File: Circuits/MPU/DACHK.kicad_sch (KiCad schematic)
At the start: 29 parts, among them J12 Conn_02x03_Odd_Even, U1 ProASIC, U11 AD5328, U12 MAX308CSE+, U13 MAX308CSE+, U14 ADA4805-2ARMZ, U15 AD7984BRMZ

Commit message: LVDS I/F for HV
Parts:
- U1: desc FPGA -> FPGA; manf# (none) -> A3PE3000-FGG484
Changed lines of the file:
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@@
 			)
 		)
-		(property "Datasheet" "	https://www.microsemi.com/document-portal/doc_download/130701-ds0098-proasic3e-flash-family-fpgas-datasheet"
+		(property "Datasheet" "https://www.microsemi.com/document-portal/doc_download/130701-ds0098-proasic3e-flash-family-fpgas-datasheet"
 			(at 30.48 87.63 0)
 			(effects
@@
 			)
 		)
-		(property "desc" "	FPGA"
+		(property "desc" "FPGA"
 			(at 30.48 90.17 0)
 			(effects
@@
 			)
 		)
+		(property "manf#" "A3PE3000-FGG484"
+			(at 30.48 85.09 0)
+			(effects
+				(font
+					(size 1.27 1.27)
+				)
+				(justify left)
+				(hide yes)
+			)
+		)
 		(pin "T16"
 		)
@@
 		)
 		(pin "AB8"
+		)
+		(pin "P19"
+		)
+		(pin "P21"
+		)
+		(pin "R19"
+		)
+		(pin "R21"
+		)
+		(pin "T20"
+		)
+		(pin "T21"
+		)
+		(pin "U20"
+		)
+		(pin "U21"
+		)
+		(pin "V21"
+		)
+		(pin "W21"
 		)
 		(instances
@@
 			)
 		)
-		(property "Datasheet" "	https://www.microsemi.com/document-portal/doc_download/130701-ds0098-proasic3e-flash-family-fpgas-datasheet"
+		(property "Datasheet" "https://www.microsemi.com/document-portal/doc_download/130701-ds0098-proasic3e-flash-family-fpgas-datasheet"
 			(at 248.92 143.51 0)
 			(effects
@@
 			)
 		)
-		(property "desc" "	FPGA"
+		(property "desc" "FPGA"
 			(at 248.92 146.05 0)
 			(effects
@@
 			)
 		)
+		(property "manf#" "A3PE3000-FGG484"
+			(at 248.92 140.97 0)
+			(effects
+				(font
+					(size 1.27 1.27)
+				)
+				(justify left)
+				(hide yes)
+			)
+		)
 		(pin "A12"
 		)
@@
 		(pin "A8"
 		)
+		(pin "P19"
+		)
+		(pin "P21"
+		)
+		(pin "R19"
+		)
+		(pin "R21"
+		)
+		(pin "T20"
+		)
+		(pin "T21"
+		)
+		(pin "U20"
+		)
+		(pin "U21"
+		)
+		(pin "V21"
+		)
+		(pin "W21"
+		)
 		(instances

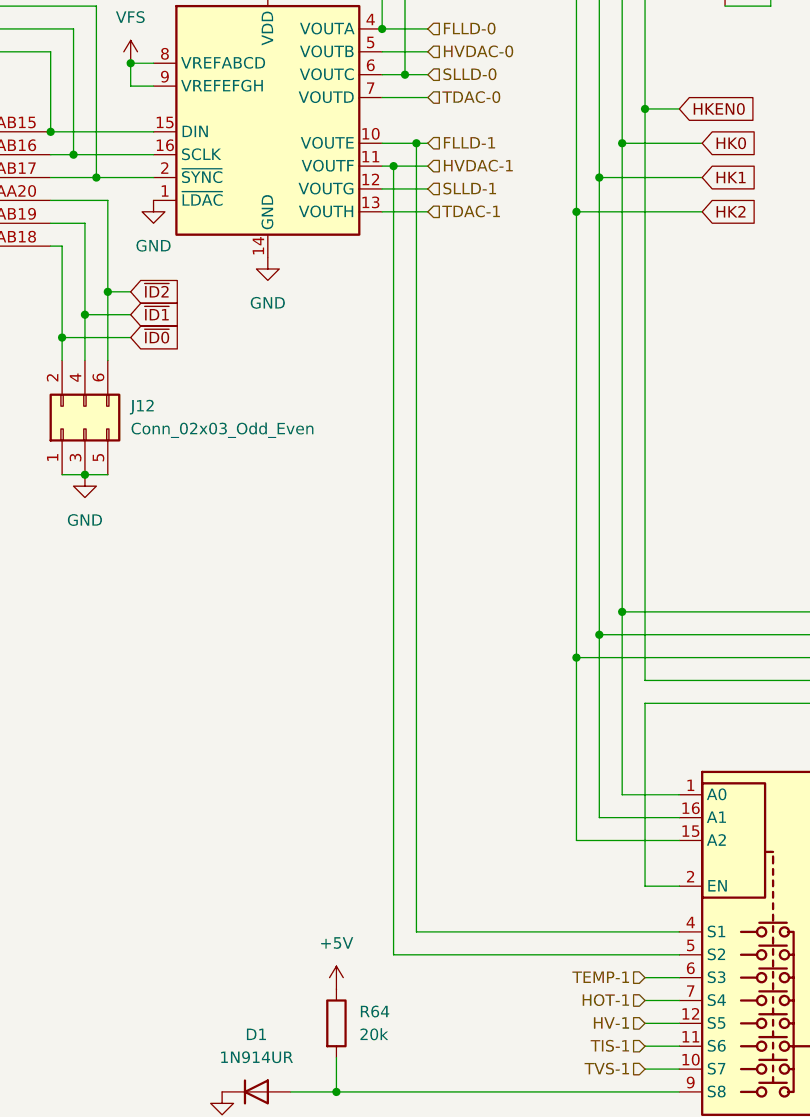
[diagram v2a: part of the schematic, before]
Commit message: Fix errors found by Norm Dobson
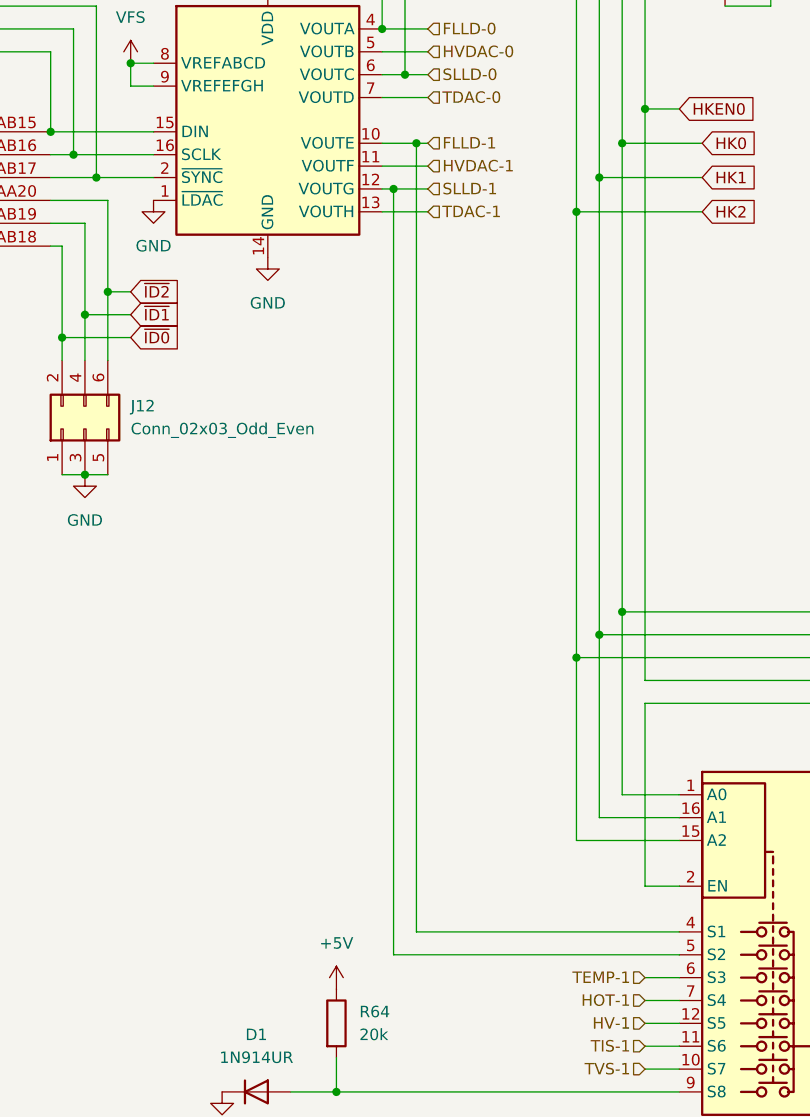
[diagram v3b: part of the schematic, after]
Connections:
- net HVDAC-1: no longer U12.5 (S2)
- net SLLD-1: now also U12.5 (S2)
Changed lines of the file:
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@@
-	)
-	(junction
-		(at 76.2 87.63)
-		(diameter 0)
-		(color 0 0 0 0)
 	)
 	(junction
@@
 	)
 	(junction
+		(at 76.2 90.17)
+		(diameter 0)
+		(color 0 0 0 0)
+	)
+	(junction
 		(at 152.4 99.06)
 		(diameter 0)
@@
 	(wire
 		(pts
-			(xy 80.01 87.63) (xy 76.2 87.63)
-		)
-		(stroke
-			(width 0)
-			(type default)
-		)
-	)
-	(wire
-		(pts
 			(xy 241.3 134.62) (xy 254 134.62)
 		)
@@
 	(wire
 		(pts
-			(xy 80.01 90.17) (xy 74.93 90.17)
+			(xy 80.01 90.17) (xy 76.2 90.17)
 		)
 		(stroke
@@
 	(wire
 		(pts
+			(xy 76.2 90.17) (xy 76.2 175.26)
+		)
+		(stroke
+			(width 0)
+			(type default)
+		)
+	)
+	(wire
+		(pts
 			(xy 222.25 149.86) (xy 222.25 139.7)
 		)
@@
 	(wire
 		(pts
-			(xy 76.2 87.63) (xy 74.93 87.63)
+			(xy 74.93 87.63) (xy 80.01 87.63)
 		)
 		(stroke
@@
 	(wire
 		(pts
-			(xy 76.2 175.26) (xy 76.2 87.63)
-		)
-		(stroke
-			(width 0)
-			(type default)
-		)
-	)
-	(wire
-		(pts
 			(xy 241.3 85.09) (xy 247.65 85.09)
 		)
@@
 		)
 		(stroke
+			(width 0)
+			(type default)
+		)
+	)
+	(wire
+		(pts
+			(xy 76.2 90.17) (xy 74.93 90.17)
+		)
+		(stroke
